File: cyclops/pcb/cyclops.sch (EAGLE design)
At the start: 141 parts, among them Q1 BC817, Q2 IRF510, Q3 BC817, T0 0, T1 0, T2 0, T3 0, U1 MCP4921, U10 TLV2374, U11 THS4281, U12 MAX4564, U13 ZXTD, U14 ZXTD, U2 ADG3301, U3 MAX4564, U4 LT1931, U5 LT1764A, U6 337L, U7 TLV3701, U8 ADR03, U9 OP1177, X1 SLP3, X2 SLP3, X3 SLP3

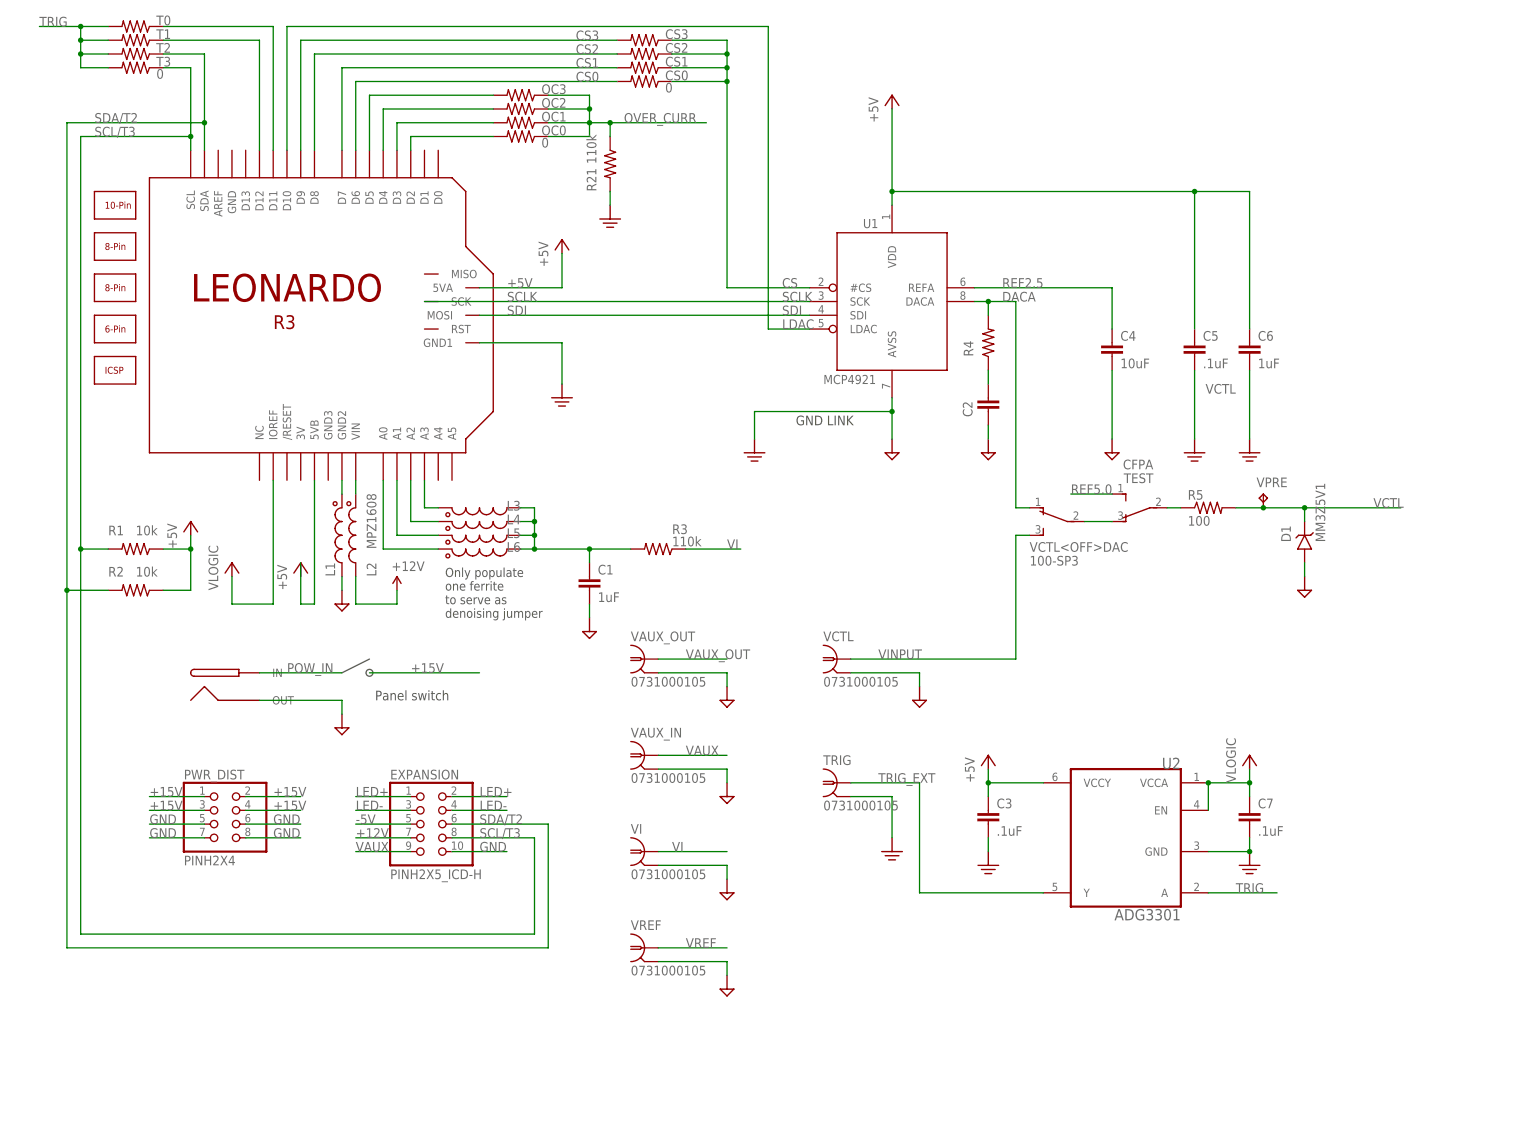
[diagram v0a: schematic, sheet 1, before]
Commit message: Started PCB modifications for Rev3.6.
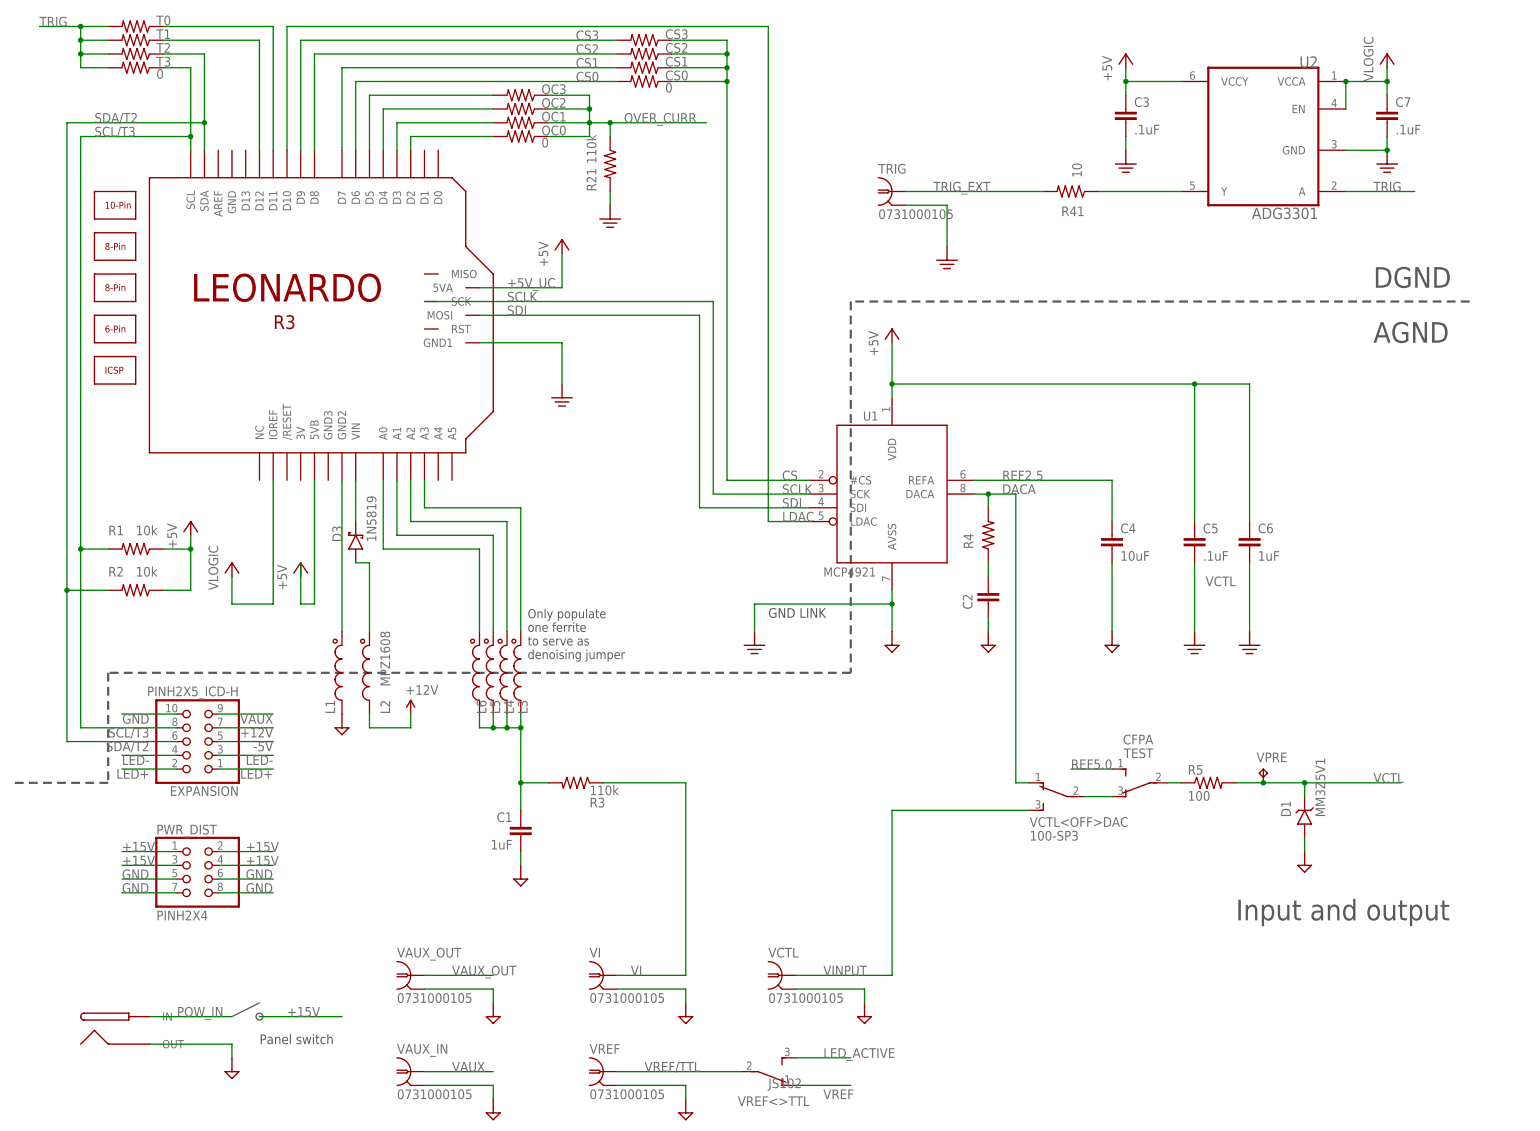
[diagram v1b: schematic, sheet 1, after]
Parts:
- removed 1AMP: RED, cyclops:LED_0603
- removed PWR: BLUE, cyclops:LED_0603
- removed X1, X2, X3: SLP3, cyclops:LIGHT-PIPE_SL30-150-100-F
- added +5V: TPTP16R, cyclops:TPTP16R
- added C37, C38: 1uF, cyclops:C_0805
- added C40, C8: .1uF, cyclops:C_0603
- added D3: 1N5819, jonnew:S-DIODESOD-123
- added IND: (no value), jonnew:LED_2X_VERTICAL
- added Q4: BC817, cyclops:BC817-16SMD
- added R38: 200, cyclops:R_0603
- added R40, R44: 100k, cyclops:R_0603
- added R41: 10, cyclops:R_0603
- added R42: 1k, cyclops:R_0603
- added R43: 10k, cyclops:R_0603
- added U67: MCP1702, jonnew:LDO-FIXED_MCP1702
- added U69: LT1716, jonnew:COMPARITOR_LT1716
- added VREF<>TTL: JS102, cyclops:SPDT_JS
- OC: value RED -> (none); device cyclops:LED_0603 -> jonnew:LED_2X_VERTICAL
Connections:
- removed net N$38: OC.C, Q3.C
- new net +5V_UC: C3.1, C5.1, C6.1, LEONARDO.5VA, LEONARDO.5VB, R1.1, R2.1, U1.VDD, U2.VCCY
- new net GND1: Q4.E
- new net LED_ACTIVE: VREF<>TTL.3
- new net N$42: R38.1, R40.1, R44.2, U69G$1.+IN
- new net N$43: D3.A, L2.1
- new net N$46: IND2.A, R42.1
- new net N$47: IND2.C, Q4.C
- new net N$49: Q4.B, R43.1
- new net N$50: R41.1, U2.Y
- new net OC: OC2.C, Q3.C
- new net VREF/TTL: VREF.1, VREF<>TTL.2
- new net ~LED_ACTIVE: R38.2, R43.2, U69G$1.OUT
- net +12V: now also C38.1, R42.2, U67.VI
- net +5V: now also +5V.TP, C37.1, C8.1, R40.2, U67.VO, U69G$2.V+; no longer C3.1, C5.1, C6.1, LEONARDO.5VA, LEONARDO.5VB, R1.1, R2.1, U1.VDD, U2.VCCY
- net GND: now also C37.2, C38.2, C40.2, C8.2, IND1.C, R44.1, U67.GND, U69G$2.V-; no longer L1.2, PWR.C
- net LED-: now also U69G$1.-IN
- net N$16: now also OC2.A; no longer OC.A
- net N$2: now also OC1.A; no longer 1AMP.A
- net N$3: now also IND1.A; no longer PWR.A
- net N$5: now also C40.1
- net N$9: now also OC1.C; no longer 1AMP.C
- net TRIG_EXT: now also R41.2; no longer U2.Y
- net VIN_ARDUINO: now also D3.C; no longer L2.1
- net VREF: now also VREF<>TTL.1; no longer VREF.1
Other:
- note added: "DRIVETRAIN"
- note added: "Input offset of TLV2374 is 6.5 mV max. At unity gain, we should not get spurious triggers with a ref of 10 mV"
- note added: "LED ACTIVE [TEST!]"
- note added: "OVERCURRENT WARNING"
- note added: "VOLTAGE REFERENCES"
- note removed: "2.5 Volt Reference"
- note removed: "5 Volt Reference"
- note removed: "Drivetrain"
- note removed: "Overcurrent warning"
- moved on the sheet: C1, C13, C18, C19, C2, C3, C4, C5, C6, C7, D1, EXPANSION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
